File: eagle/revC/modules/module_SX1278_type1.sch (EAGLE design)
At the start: 17 parts, among them X1 734120110

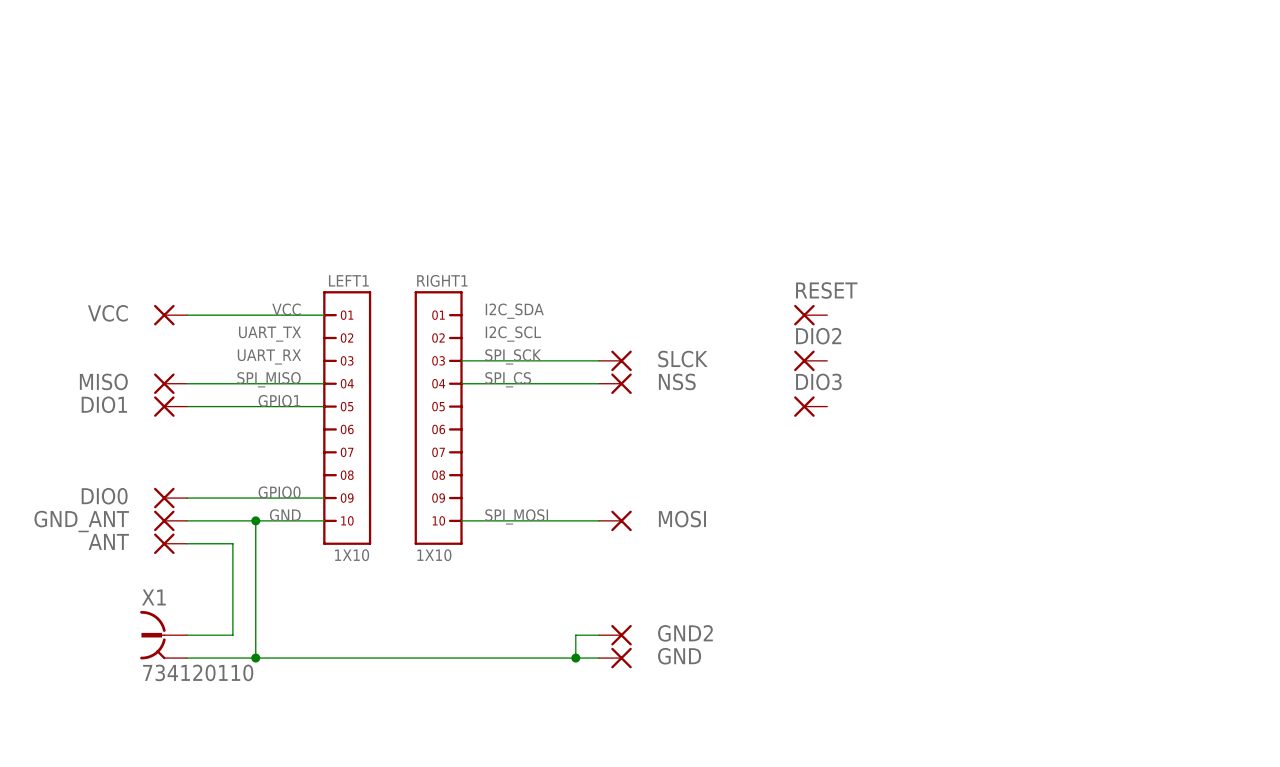
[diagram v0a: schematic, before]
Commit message: Replaced modules with library parts
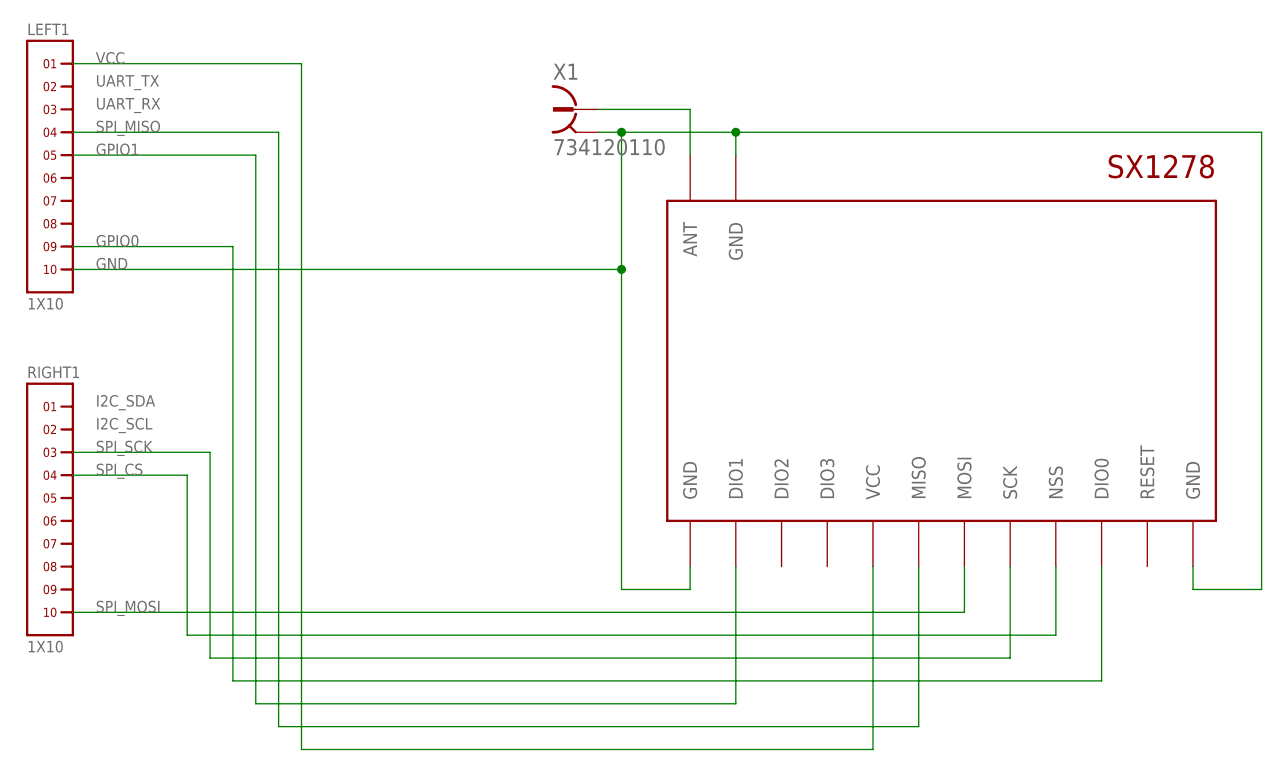
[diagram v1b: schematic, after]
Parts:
- removed ANT, DIO0, DIO1, DIO2, DIO3, GND, GND2, GND_ANT, MISO, MOSI, NSS, RESET, SLCK, VCC: (no value), wirepad:SMD1
- added U$1: SX1278_1, RadioShield:SX1278_1
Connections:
- removed net ANT: ANT.P, X1.1
- removed net INT0: DIO0.P, LEFT1.9
- removed net INT1: DIO1.P, LEFT1.5
- removed net SPI_CS: NSS.P, RIGHT1.4
- removed net SPI_MISO: LEFT1.4, MISO.P
- removed net SPI_MOSI: MOSI.P, RIGHT1.10
- removed net SPI_SCK: RIGHT1.3, SLCK.P
- removed net VCC: LEFT1.1, VCC.P
- new net N$1: U$1.ANT, X1.1
- new net N$2: RIGHT1.10, U$1.MOSI
- new net N$3: RIGHT1.4, U$1.NSS
- new net N$4: RIGHT1.3, U$1.SCK
- new net N$5: LEFT1.9, U$1.DIO0
- new net N$6: LEFT1.5, U$1.DIO1
- new net N$7: LEFT1.4, U$1.MISO
- new net N$8: LEFT1.1, U$1.VCC
- net GND: now also U$1.GND@1, U$1.GND@2, U$1.GND@3; no longer GND.P, GND2.P, GND_ANT.P
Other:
- moved on the sheet: LEFT1, RIGHT1, X1
